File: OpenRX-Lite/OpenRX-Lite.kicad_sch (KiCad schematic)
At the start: 0 parts

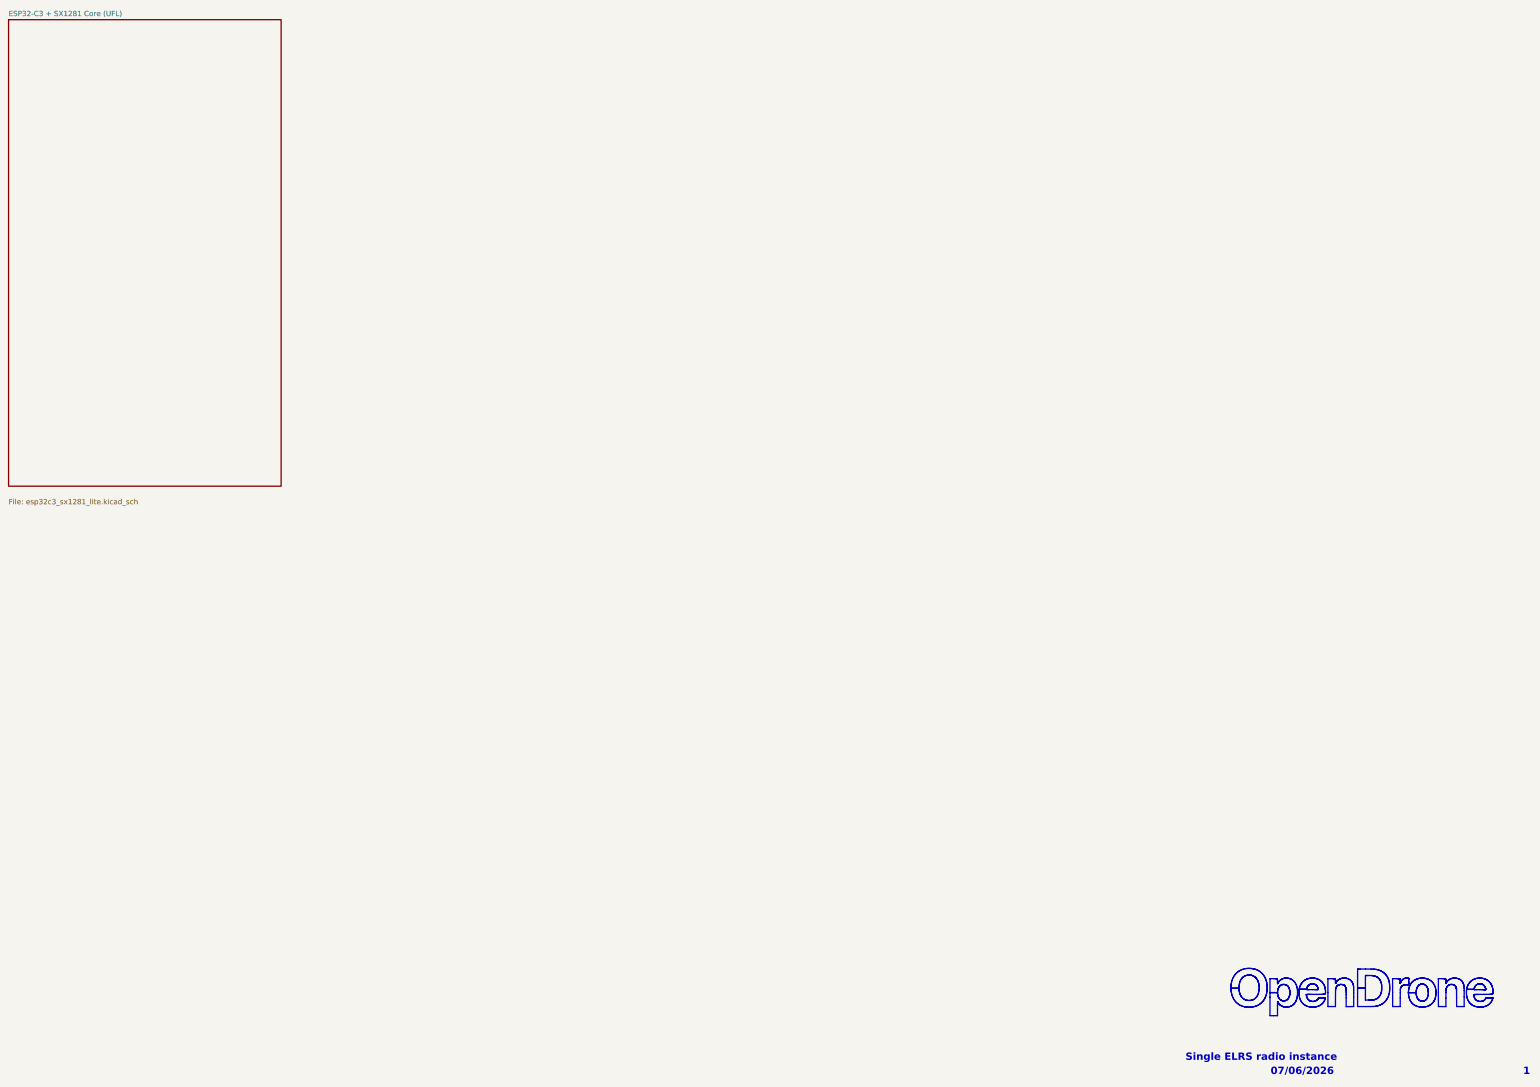
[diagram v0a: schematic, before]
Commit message: feat(OpenRX-Lite): convert to AntAIO antweight battlebot AIO
Extend OpenRX-Lite (ESP32-C3 + SX1281 ELRS RX) into an integrated
1–2S antweight combat-robot controller in the Malenki-Nano style:

- Triple brushed-DC ESC: 3× DRV8212 (U6/U10 drive, U11 weapon)
- 6-axis IMU LSM6DS3TR-C (U2) on the shared radio SPI bus
- Power: TPS63070 buck-boost (+BATT→5V) + TLV75533 LDO (→3V3),
  AON7407 reverse-polarity P-FET
- New footprints/3D: DFN-8, WSON-8, VQFN-15, LGA-14, SOD-923, IND 2.0×1.6
- Add part datasheets (DRV8212, LSM6DS3TR-C, TPS63070, AON7407)
- CHANGELIST.md: verified open/done items
- REVIEW.md: multi-agent pin/datasheet/electrical design review

Co-Authored-By: Claude Opus 4.8 (1M context) <noreply@anthropic.com>
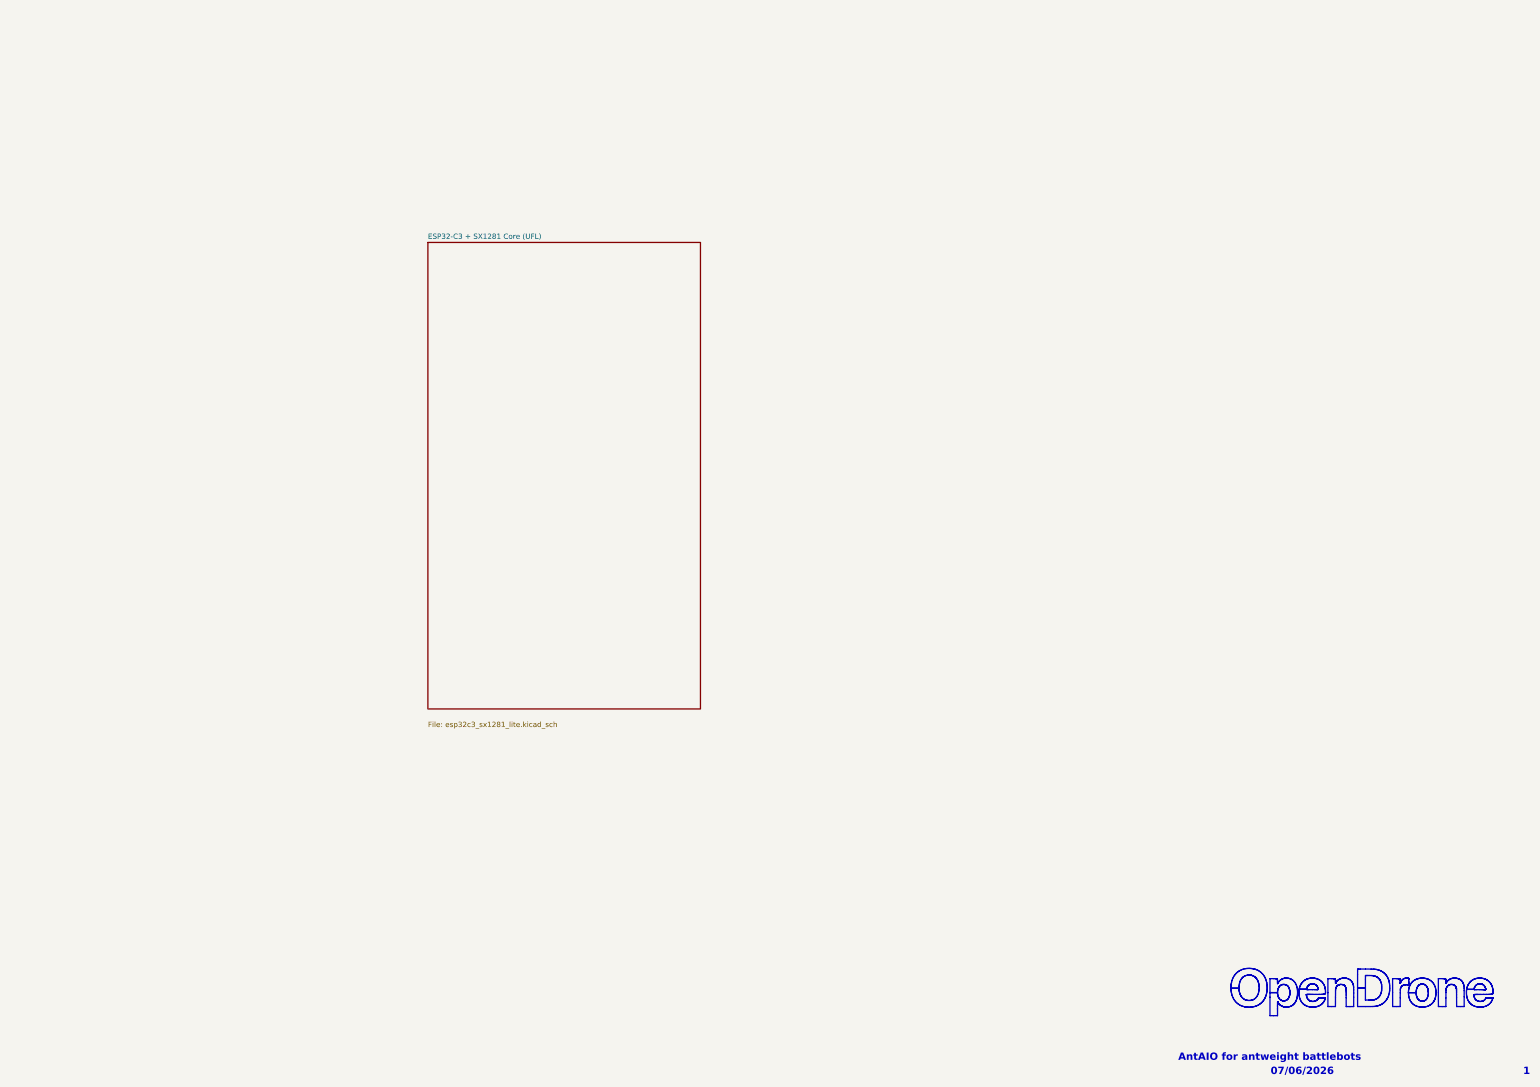
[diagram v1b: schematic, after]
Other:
- note added: "AntAIO for antweight battlebots"
- note removed: "Single ELRS radio instance"
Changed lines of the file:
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@@
 		)
 	)
-	(text "Single ELRS radio instance"
+	(text "AntAIO for antweight battlebots"
 		(exclude_from_sim no)
-		(at 328.93 276.86 0)
+		(at 330.962 276.86 0)
 		(effects
 			(font
@@
 	)
 	(sheet
-		(at 25.4 25.4)
+		(at 127 79.375)
 		(size 66.04 113.03)
 		(exclude_from_sim no)
@@
 		)
 		(property "Sheetname" "ESP32-C3 + SX1281 Core (UFL)"
-			(at 25.4 24.6888 0)
+			(at 127 78.6638 0)
 			(show_name no)
 			(do_not_autoplace no)
@@
 		)
 		(property "Sheetfile" "esp32c3_sx1281_lite.kicad_sch"
-			(at 25.4 141.478 0)
+			(at 127 195.453 0)
 			(show_name no)
 			(do_not_autoplace no)
